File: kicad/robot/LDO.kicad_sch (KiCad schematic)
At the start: 17 parts, among them U14 MAX77642ANA+

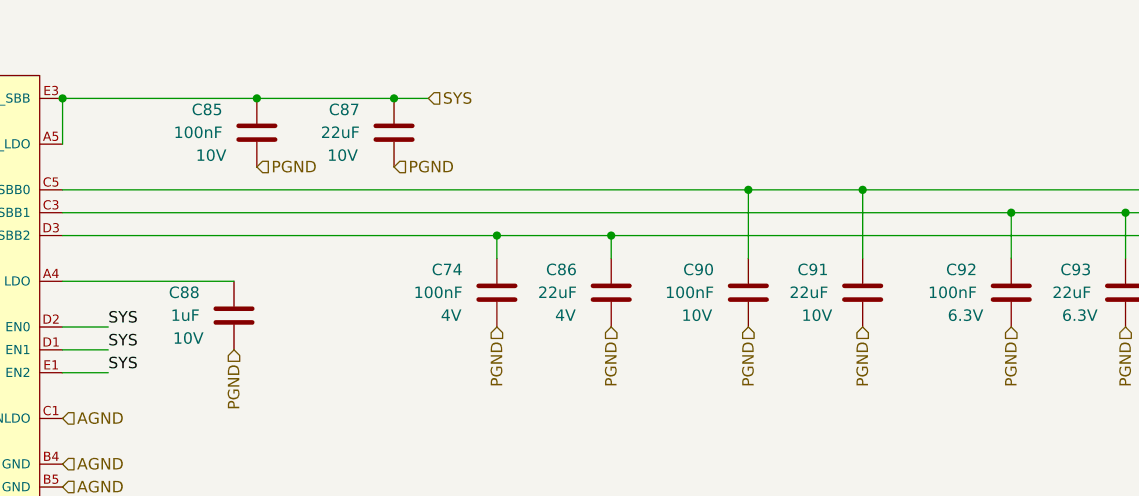
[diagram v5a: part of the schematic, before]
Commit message: bulk footprint updates to capacitors
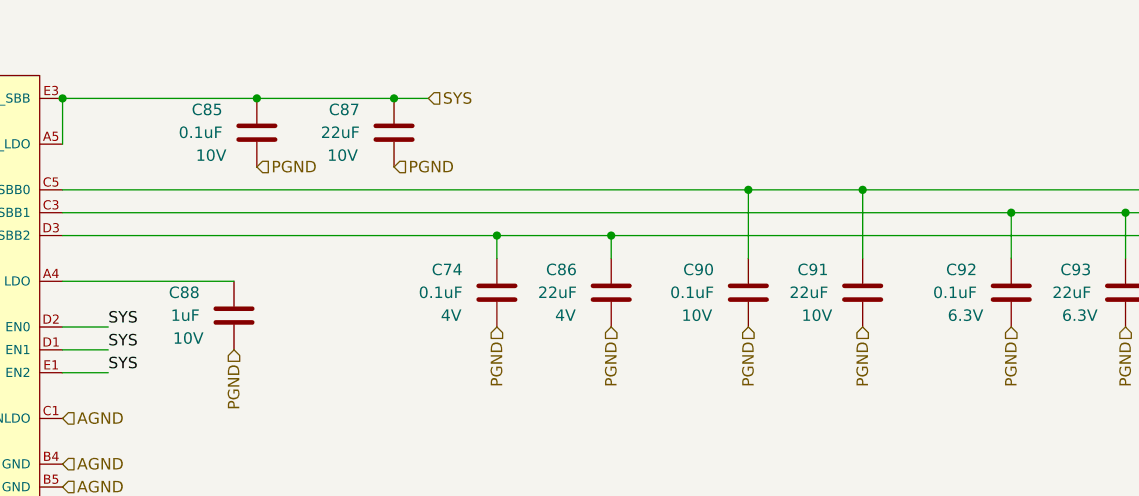
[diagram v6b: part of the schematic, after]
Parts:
- C4, C88: footprint Capacitor_SMD:C_0603_1608Metric -> Capacitor_SMD:C_0402_1005Metric
- C74, C85, C90, C92: value 100nF -> 0.1uF; footprint Capacitor_SMD:C_0603_1608Metric -> Capacitor_SMD:C_0402_1005Metric
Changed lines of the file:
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@@
       (effects (font (size 1.27 1.27)) (justify left))
     )
-    (property "Footprint" "Capacitor_SMD:C_0603_1608Metric" (id 2) (at 155.2448 104.14 0)
+    (property "Footprint" "Capacitor_SMD:C_0402_1005Metric" (id 2) (at 155.2448 104.14 0)
       (effects (font (size 1.27 1.27)) hide)
     )
@@
       (effects (font (size 1.27 1.27)) (justify left))
     )
-    (property "Value" "100nF" (id 1) (at 181.61 97.7899 0)
-      (effects (font (size 1.27 1.27)) (justify left))
-    )
-    (property "Footprint" "Capacitor_SMD:C_0603_1608Metric" (id 2) (at 184.4548 101.6 0)
+    (property "Value" "0.1uF" (id 1) (at 181.61 97.7899 0)
+      (effects (font (size 1.27 1.27)) (justify left))
+    )
+    (property "Footprint" "Capacitor_SMD:C_0402_1005Metric" (id 2) (at 184.4548 101.6 0)
       (effects (font (size 1.27 1.27)) hide)
     )
@@
       (effects (font (size 1.27 1.27)) (justify left))
     )
-    (property "Value" "100nF" (id 1) (at 154.94 80.0099 0)
-      (effects (font (size 1.27 1.27)) (justify left))
-    )
-    (property "Footprint" "Capacitor_SMD:C_0603_1608Metric" (id 2) (at 157.7848 83.82 0)
+    (property "Value" "0.1uF" (id 1) (at 154.94 80.0099 0)
+      (effects (font (size 1.27 1.27)) (justify left))
+    )
+    (property "Footprint" "Capacitor_SMD:C_0402_1005Metric" (id 2) (at 157.7848 83.82 0)
       (effects (font (size 1.27 1.27)) hide)
     )
@@
       (effects (font (size 1.27 1.27)) (justify left))
     )
-    (property "Footprint" "Capacitor_SMD:C_0603_1608Metric" (id 2) (at 66.3448 83.82 0)
+    (property "Footprint" "Capacitor_SMD:C_0402_1005Metric" (id 2) (at 66.3448 83.82 0)
       (effects (font (size 1.27 1.27)) hide)
     )
@@
       (effects (font (size 1.27 1.27)) (justify left))
     )
-    (property "Value" "100nF" (id 1) (at 238.76 97.7899 0)
-      (effects (font (size 1.27 1.27)) (justify left))
-    )
-    (property "Footprint" "Capacitor_SMD:C_0603_1608Metric" (id 2) (at 241.6048 101.6 0)
+    (property "Value" "0.1uF" (id 1) (at 238.76 97.7899 0)
+      (effects (font (size 1.27 1.27)) (justify left))
+    )
+    (property "Footprint" "Capacitor_SMD:C_0402_1005Metric" (id 2) (at 241.6048 101.6 0)
       (effects (font (size 1.27 1.27)) hide)
     )
@@
       (effects (font (size 1.27 1.27)) (justify left))
     )
-    (property "Value" "100nF" (id 1) (at 209.55 97.7899 0)
-      (effects (font (size 1.27 1.27)) (justify left))
-    )
-    (property "Footprint" "Capacitor_SMD:C_0603_1608Metric" (id 2) (at 212.3948 101.6 0)
-      (effects (font (size 1.27 1.27)) hide)
-    )
+    (property "Value" "0.1uF" (id 1) (at 209.55 97.7899 0)
+      (effects (font (size 1.27 1.27)) (justify left))
+    )
+    (property "Footprint" "Capacitor_SMD:C_0402_1005Metric" (id 2) (at 212.3948 101.6 0)
+      (effects (font (size 1.27 1.27)) hide)
+    )

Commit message: Bulk BOM edits and one replaced footprint for U15
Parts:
- C4, C88: Manufacturer (none) -> Murata; Part Number (none) -> GRM155R61E105KA12D
- C74, C85, C90, C92: Manufacturer (none) -> Samsung; Part Number (none) -> CL05A104KA5NNNC
- C84: Manufacturer (none) -> Samsung; Part Number (none) -> CL05B103KA5NNNC
- C86, C87, C91, C93: Manufacturer (none) -> Murata; Part Number (none) -> GRM188R61A226ME15D
- R53: Manufacturer Panasonic -> Stackpole Electronics; Part Number ERJ-1GEF1133C -> RMCF0603FT113K
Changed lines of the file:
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@@
     )
     (property "Description" "%1" (id 4) (at 72.39 121.92 0))
-    (property "Manufacturer" "Panasonic" (id 5) (at 68.58 118.11 0)
-      (effects (font (size 1.27 1.27)) hide)
-    )
-    (property "Part Number" "ERJ-1GEF1133C" (id 6) (at 68.58 118.11 0)
+    (property "Manufacturer" "Stackpole Electronics" (id 5) (at 68.58 118.11 0)
+      (effects (font (size 1.27 1.27)) hide)
+    )
+    (property "Part Number" "RMCF0603FT113K" (id 6) (at 68.58 118.11 0)
       (effects (font (size 1.27 1.27)) hide)
     )
@@
     )
     (property "Description" "6.3V" (id 4) (at 250.19 100.33 0))
+    (property "Manufacturer" "Murata" (id 5) (at 255.27 97.79 0)
+      (effects (font (size 1.27 1.27)) hide)
+    )
+    (property "Part Number" "GRM188R61A226ME15D" (id 6) (at 255.27 97.79 0)
+      (effects (font (size 1.27 1.27)) hide)
+    )
     (pin "1")
     (pin "2")
@@
     )
     (property "Description" "10V" (id 4) (at 151.13 102.87 0))
+    (property "Manufacturer" "Murata" (id 5) (at 156.21 100.33 0)
+      (effects (font (size 1.27 1.27)) hide)
+    )
+    (property "Part Number" "GRM155R61E105KA12D" (id 6) (at 156.21 100.33 0)
+      (effects (font (size 1.27 1.27)) hide)
+    )
     (pin "1")
     (pin "2")
@@
     )
     (property "Description" "10V" (id 4) (at 168.275 82.55 0))
+    (property "Manufacturer" "Murata" (id 5) (at 173.99 80.01 0)
+      (effects (font (size 1.27 1.27)) hide)
+    )
+    (property "Part Number" "GRM188R61A226ME15D" (id 6) (at 173.99 80.01 0)
+      (effects (font (size 1.27 1.27)) hide)
+    )
     (pin "1")
     (pin "2")
@@
     )
     (property "Description" "4V" (id 4) (at 193.04 100.33 0))
+    (property "Manufacturer" "Murata" (id 5) (at 198.12 97.79 0)
+      (effects (font (size 1.27 1.27)) hide)
+    )
+    (property "Part Number" "GRM188R61A226ME15D" (id 6) (at 198.12 97.79 0)
+      (effects (font (size 1.27 1.27)) hide)
+    )
     (pin "1")
     (pin "2")
@@
     )
     (property "Description" "4V" (id 4) (at 180.34 100.33 0))
+    (property "Manufacturer" "Samsung" (id 5) (at 185.42 97.79 0)
+      (effects (font (size 1.27 1.27)) hide)
+    )
+    (property "Part Number" "CL05A104KA5NNNC" (id 6) (at 185.42 97.79 0)
+      (effects (font (size 1.27 1.27)) hide)
+    )
     (pin "1")
     (pin "2")
@@
     )
     (property "Description" "10V" (id 4) (at 153.67 82.55 0))
+    (property "Manufacturer" "Samsung" (id 5) (at 158.75 80.01 0)
+      (effects (font (size 1.27 1.27)) hide)
+    )
+    (property "Part Number" "CL05A104KA5NNNC" (id 6) (at 158.75 80.01 0)
+      (effects (font (size 1.27 1.27)) hide)
+    )
     (pin "1")
     (pin "2")
@@
     )
     (property "Description" "10V" (id 4) (at 62.23 82.55 0))
+    (property "Manufacturer" "Murata" (id 5) (at 67.31 80.01 0)
+      (effects (font (size 1.27 1.27)) hide)
+    )
+    (property "Part Number" "GRM155R61E105KA12D" (id 6) (at 67.31 80.01 0)
+      (effects (font (size 1.27 1.27)) hide)
+    )
     (pin "1")
     (pin "2")
@@
     )
     (property "Description" "6.3V" (id 4) (at 237.49 100.33 0))
+    (property "Manufacturer" "Samsung" (id 5) (at 242.57 97.79 0)
+      (effects (font (size 1.27 1.27)) hide)
+    )
+    (property "Part Number" "CL05A104KA5NNNC" (id 6) (at 242.57 97.79 0)
+      (effects (font (size 1.27 1.27)) hide)
+    )
     (pin "1")
     (pin "2")
@@
     )
     (property "Description" "10V" (id 4) (at 220.98 100.33 0))
+    (property "Manufacturer" "Murata" (id 5) (at 226.06 97.79 0)
+      (effects (font (size 1.27 1.27)) hide)
+    )
+    (property "Part Number" "GRM188R61A226ME15D" (id 6) (at 226.06 97.79 0)
+      (effects (font (size 1.27 1.27)) hide)
+    )
     (pin "1")
     (pin "2")
@@
     )
     (property "Description" "10V" (id 4) (at 207.645 100.33 0))
+    (property "Manufacturer" "Samsung" (id 5) (at 213.36 97.79 0)
+      (effects (font (size 1.27 1.27)) hide)
+    )
+    (property "Part Number" "CL05A104KA5NNNC" (id 6) (at 213.36 97.79 0)
+      (effects (font (size 1.27 1.27)) hide)
+    )
     (pin "1")
     (pin "2")
@@
     )
     (property "Description" "10V" (id 4) (at 85.725 90.805 90))
-    (pin "1")
-    (pin "2")
+    (property "Manufacturer" "Samsung" (id 5) (at 85.725 93.98 0)
+      (effects (font (size 1.27 1.27)) hide)
+    )
+    (property "Part Number" "CL05B103KA5NNNC" (id 6) (at 85.725 93.98 0)
+      (effects (font (size 1.27 1.27)) hide)
+    )
+    (pin "1")
+    (pin "2")
